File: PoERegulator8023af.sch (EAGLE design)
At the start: 9 parts, among them J1 SJCN

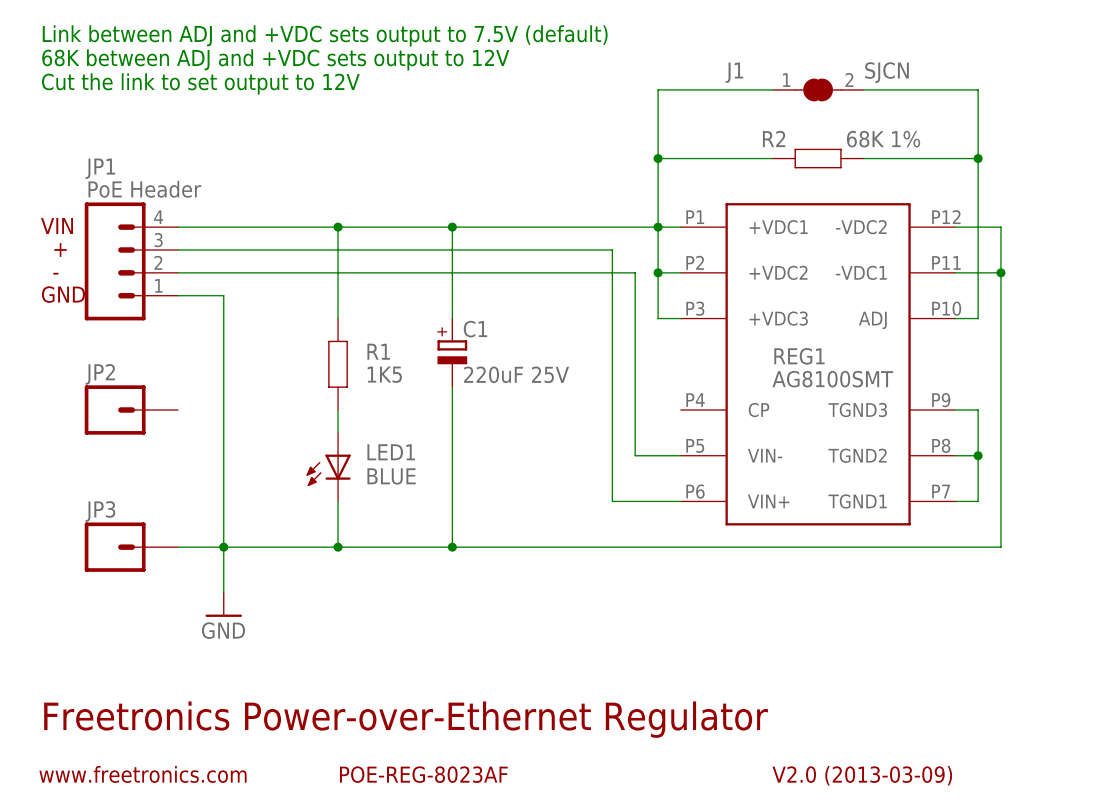
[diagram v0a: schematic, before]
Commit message: Replaced Silvertel AG8112M with AG9812M for v2.0 release
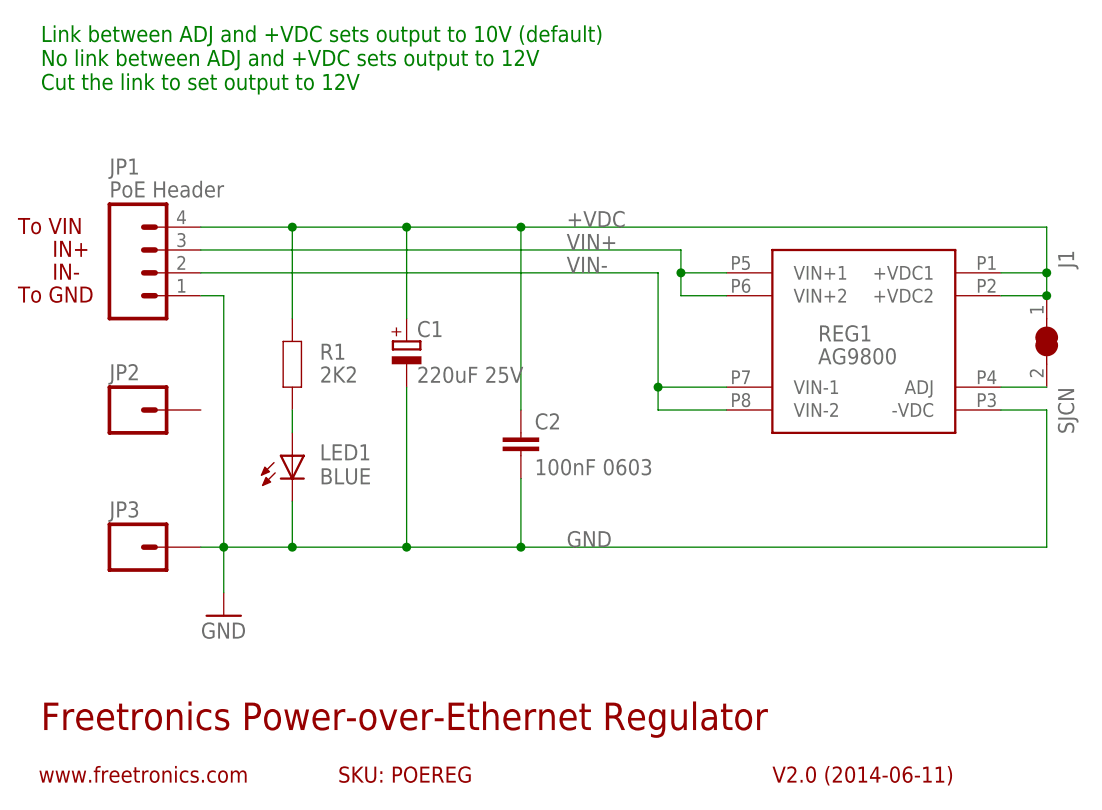
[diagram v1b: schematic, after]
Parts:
- removed R2: 68K 1%, freetronics:RESISTOR0603
- added C2: 100nF 0603, freetronics-master-v1.1:CAP0603
- R1: value 1K5 -> 2K2
- REG1: value AG8100SMT -> AG9800; device freetronics-master-v1:AG8100SMT -> freetronics-jon:AG9800
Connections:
- removed net N$2: J1.2, R2.2, REG1.ADJ
- removed net N$5: JP1.2, REG1.VIN-
- removed net TGND: REG1.TGND1, REG1.TGND2, REG1.TGND3
- removed net VIN: C1.+, J1.1, JP1.4, R1.1, R2.1, REG1.+VDC1, REG1.+VDC2, REG1.+VDC3
- new net +VDC: C1.+, C2.1, J1.1, JP1.4, R1.1, REG1.+VDC1, REG1.+VDC2
- new net VIN+: JP1.3, REG1.VIN+1, REG1.VIN+2
- new net VIN-: JP1.2, REG1.VIN-1, REG1.VIN-2
- net GND: now also C2.2, REG1.-VDC; no longer REG1.-VDC1, REG1.-VDC2
- net N$1: now also J1.2, REG1.ADJ; no longer JP1.3, REG1.VIN+
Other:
- note added: "IN+"
- note added: "IN-"
- note added: "Link between ADJ and +VDC sets output to 10V (default) No link between ADJ and +VDC sets output to 12V Cut the link to set output to 12V"
- note added: "SKU: POEREG"
- note added: "To GND"
- note added: "To VIN"
- note added: "V2.0 (2014-06-11)"
- note removed: "+"
- note removed: "-"
- note removed: "GND"
- note removed: "Link between ADJ and +VDC sets output to 7.5V (default) 68K between ADJ and +VDC sets output to 12V Cut the link to set output to 12V"
- note removed: "POE-REG-8023AF"
- note removed: "V2.0 (2013-03-09)"
- note removed: "VIN"
- moved on the sheet: C1, J1, JP1, JP2, JP3, LED1, R1

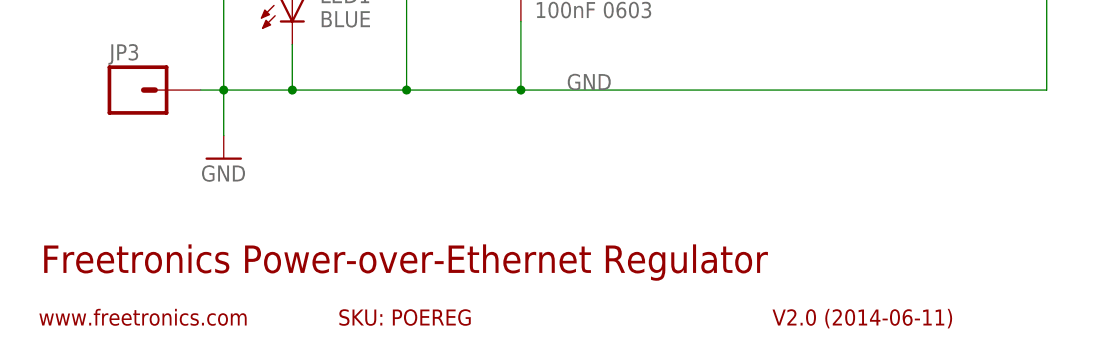
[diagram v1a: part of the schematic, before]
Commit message: Fixed fonts for silkscreen and schematic
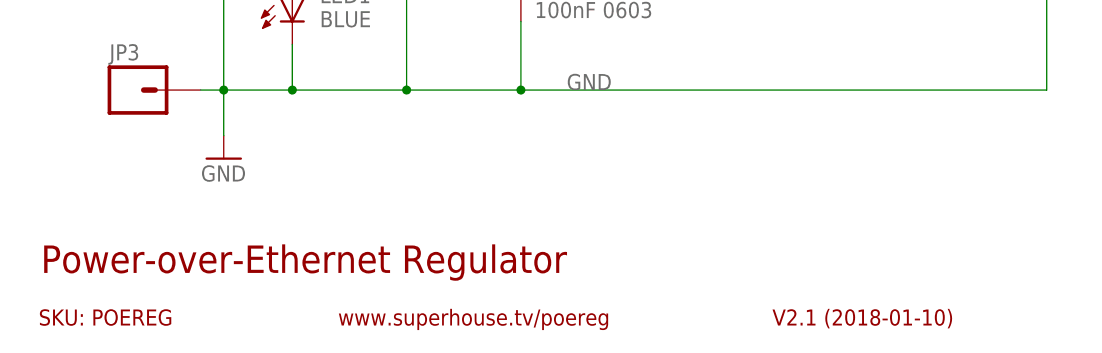
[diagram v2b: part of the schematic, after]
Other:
- note added: "Power-over-Ethernet Regulator"
- note added: "V2.1 (2018-01-10)"
- note added: "www.superhouse.tv/poereg"
- note removed: "Freetronics Power-over-Ethernet Regulator"
- note removed: "V2.0 (2014-06-11)"
- note removed: "www.freetronics.com"
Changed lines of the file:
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@@
 <?xml version="1.0" encoding="utf-8"?>
 <!DOCTYPE eagle SYSTEM "eagle.dtd">
-<eagle version="6.5.0">
+<eagle version="8.5.1">
 <drawing>
 <settings>
-<setting alwaysvectorfont="yes"/>
+<setting alwaysvectorfont="no"/>
+<setting keepoldvectorfont="yes"/>
 <setting verticaltext="up"/>
 </settings>
@@
 <sheet>
 <plain>
-<text x="7.62" y="12.7" size="3.048" layer="94">Freetronics Power-over-Ethernet Regulator</text>
-<text x="88.9" y="6.858" size="1.778" layer="94">V2.0 (2014-06-11)</text>
-<text x="7.366" y="6.858" size="1.778" layer="94">www.freetronics.com</text>
-<text x="40.64" y="6.858" size="1.778" layer="94">SKU: POEREG</text>
+<text x="7.62" y="12.7" size="3.048" layer="94">Power-over-Ethernet Regulator</text>
+<text x="88.9" y="6.858" size="1.778" layer="94">V2.1 (2018-01-10)</text>
+<text x="7.366" y="6.858" size="1.778" layer="94">SKU: POEREG</text>
+<text x="40.64" y="6.858" size="1.778" layer="94">www.superhouse.tv/poereg</text>
 <text x="5.08" y="67.818" size="1.778" layer="94">To VIN</text>
 <text x="8.89" y="65.278" size="1.778" layer="94">IN+</text>
